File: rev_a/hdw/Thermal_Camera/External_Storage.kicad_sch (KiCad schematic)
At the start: 0 parts

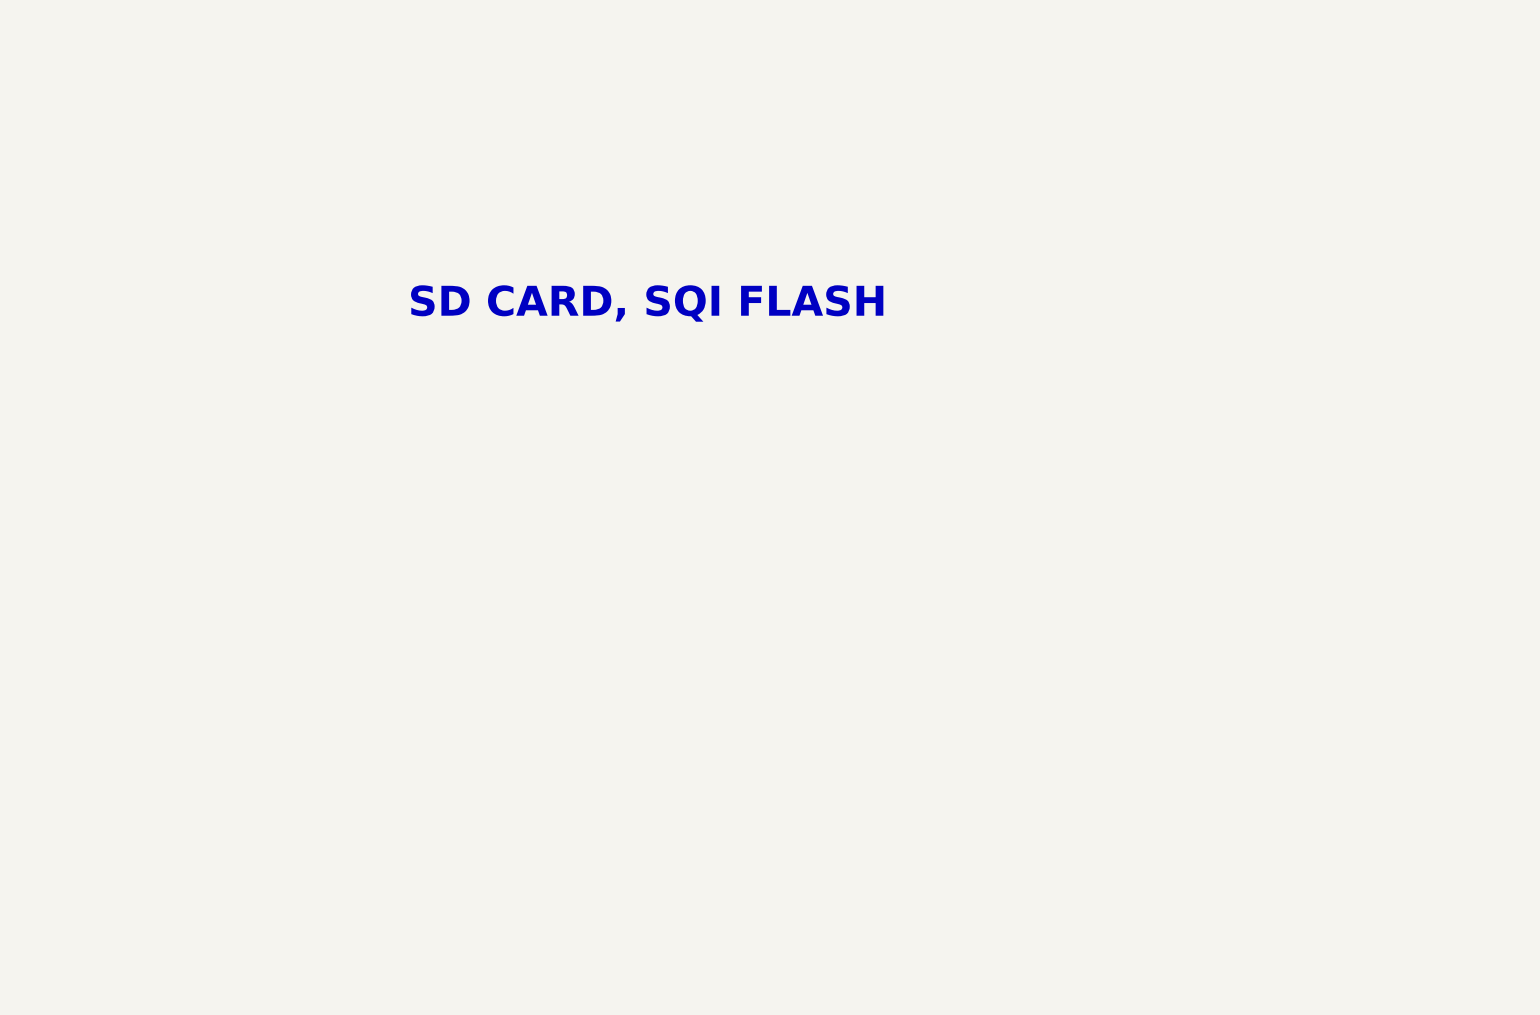
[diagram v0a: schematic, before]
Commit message: added lepton sensor, made some other schematic progress
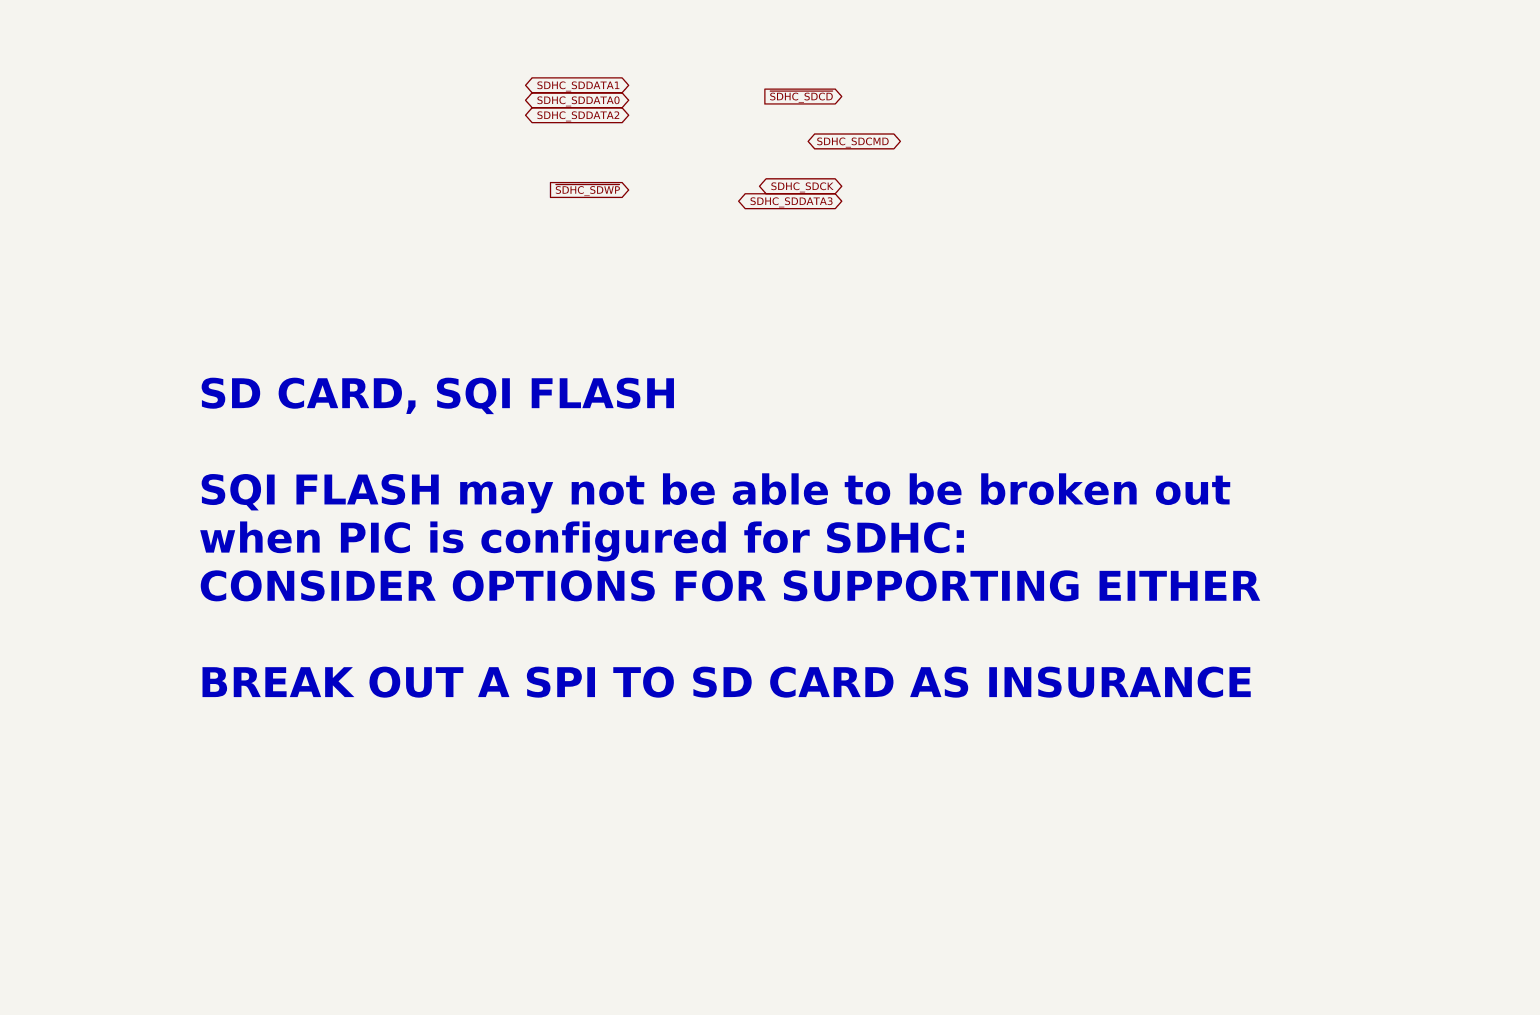
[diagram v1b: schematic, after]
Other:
- note added: "SD CARD, SQI FLASH SQI FLASH may not be able to be broken out when PIC is configured for SDHC: CONSIDER OPTIONS FOR SUPPORTING EITHER BREAK OUT A SPI TO SD CARD AS INSURANCE"
- note removed: "SD CARD, SQI FLASH"
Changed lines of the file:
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@@
   (title_block
     (title "Thermal Camera")
-    (date "2023-11-11")
+    (date "2023-11-12")
     (rev "PRELIM")
     (company "Drew Maatman and Michael Laffin")
   )
-  (text "SD CARD, SQI FLASH" (at 77.47 76.2 0)
+  (text "SD CARD, SQI FLASH\n\nSQI FLASH may not be able to be broken out\nwhen PIC is configured for SDHC:\nCONSIDER OPTIONS FOR SUPPORTING EITHER\n\nBREAK OUT A SPI TO SD CARD AS INSURANCE"
+    (at 41.91 140.97 0)
     (effects (font (face "Courier New") (size 5.08 5.08) (thickness 1.016) bold (color 194 0 0 1)) (justify left bottom))
   )
+  (global_label "~{SDHC_SDWP}" (shape input) (at 114.935 53.975 180) (fields_autoplaced)
+    (effects (font (size 1.27 1.27)) (justify right))
+    (property "Intersheetrefs" "${INTERSHEET_REFS}" (at 100.7013 53.975 0)
+      (effects (font (size 1.27 1.27)) (justify right) hide)
+    )
+  )
+  (global_label "SDHC_SDDATA1" (shape bidirectional) (at 114.935 36.195 180) (fields_autoplaced)
+    (effects (font (size 1.27 1.27)) (justify right))
+    (property "Intersheetrefs" "${INTERSHEET_REFS}" (at 96.6871 36.195 0)
+      (effects (font (size 1.27 1.27)) (justify right) hide)
+    )
+  )
+  (global_label "SDHC_SDCMD" (shape bidirectional) (at 145.415 45.72 0) (fields_autoplaced)
+    (effects (font (size 1.27 1.27)) (justify left))
+    (property "Intersheetrefs" "${INTERSHEET_REFS}" (at 162.03 45.72 0)
+      (effects (font (size 1.27 1.27)) (justify left) hide)
+    )
+  )
+  (global_label "SDHC_SDCK" (shape bidirectional) (at 151.13 53.34 180) (fields_autoplaced)
+    (effects (font (size 1.27 1.27)) (justify right))
+    (property "Intersheetrefs" "${INTERSHEET_REFS}" (at 135.9664 53.34 0)
+      (effects (font (size 1.27 1.27)) (justify right) hide)
+    )
+  )
+  (global_label "SDHC_SDDATA3" (shape bidirectional) (at 151.13 55.88 180) (fields_autoplaced)
+    (effects (font (size 1.27 1.27)) (justify right))
+    (property "Intersheetrefs" "${INTERSHEET_REFS}" (at 132.8821 55.88 0)
+      (effects (font (size 1.27 1.27)) (justify right) hide)
+    )
+  )
+  (global_label "SDHC_SDDATA0" (shape bidirectional) (at 114.935 38.735 180) (fields_autoplaced)
+    (effects (font (size 1.27 1.27)) (justify right))
+    (property "Intersheetrefs" "${INTERSHEET_REFS}" (at 96.6871 38.735 0)
+      (effects (font (size 1.27 1.27)) (justify right) hide)
+    )
+  )
+  (global_label "~{SDHC_SDCD}" (shape input) (at 151.13 38.1 180) (fields_autoplaced)
+    (effects (font (size 1.27 1.27)) (justify right))
+    (property "Intersheetrefs" "${INTERSHEET_REFS}" (at 137.0777 38.1 0)
+      (effects (font (size 1.27 1.27)) (justify right) hide)
+    )
+  )
+  (global_label "SDHC_SDDATA2" (shape bidirectional) (at 114.935 41.275 180) (fields_autoplaced)
+    (effects (font (size 1.27 1.27)) (justify right))
+    (property "Intersheetrefs" "${INTERSHEET_REFS}" (at 96.6871 41.275 0)
+      (effects (font (size 1.27 1.27)) (justify right) hide)
+    )
+  )
 )

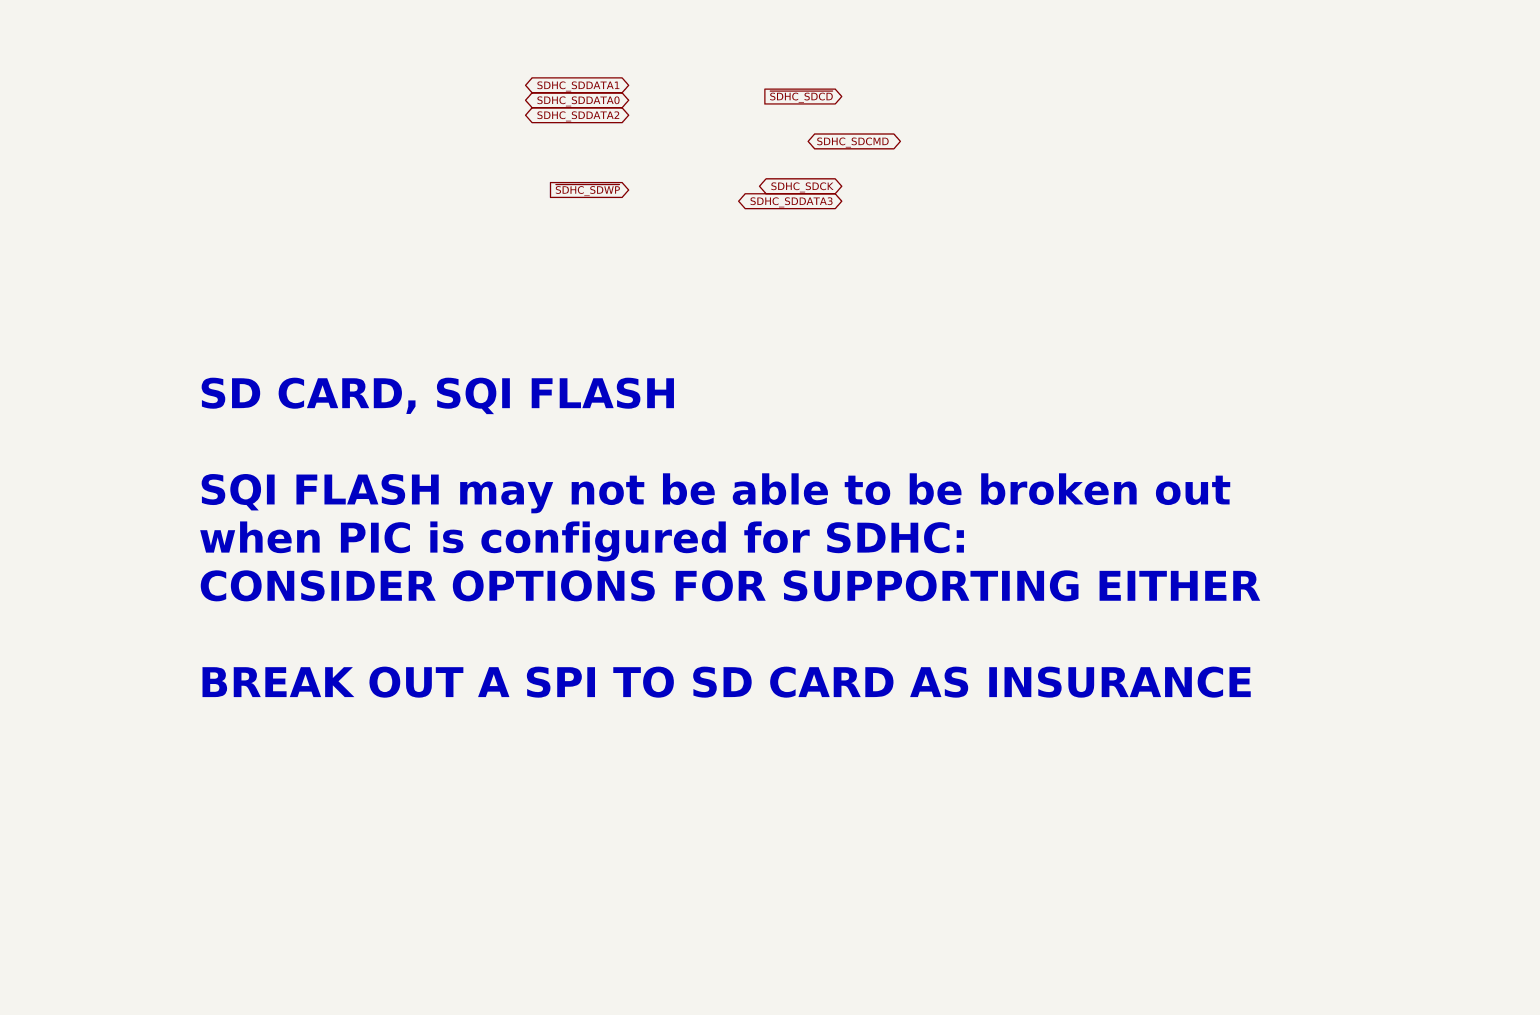
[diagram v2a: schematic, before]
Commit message: added SPI Flash and SD Card
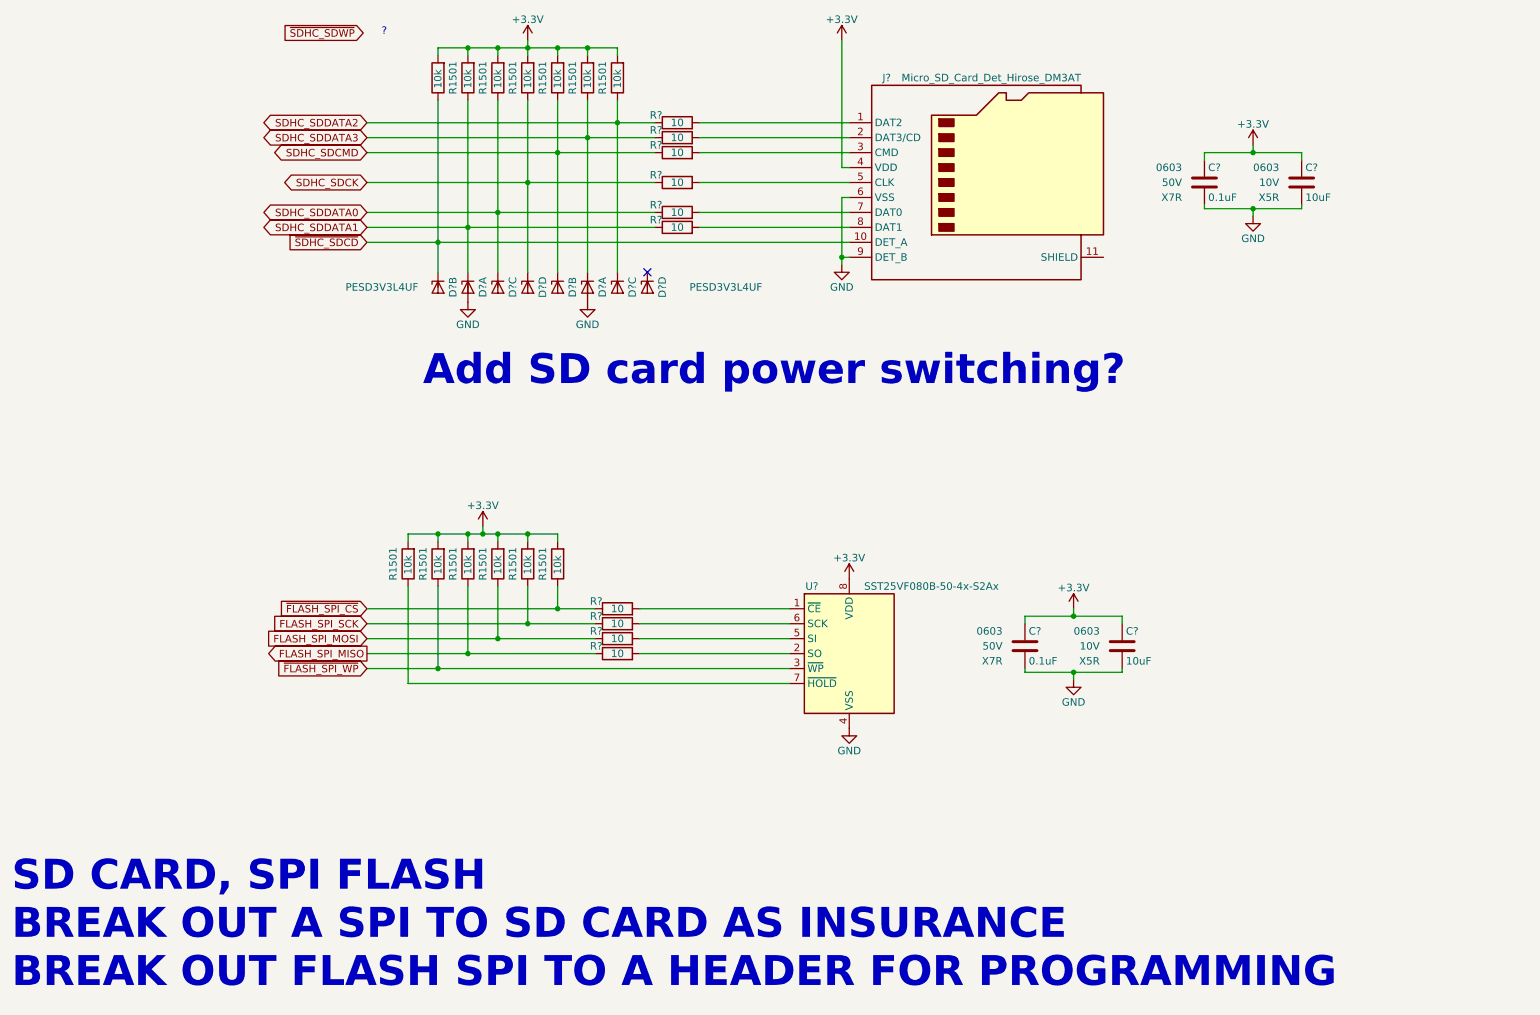
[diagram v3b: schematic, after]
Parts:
- added C? (x2): 10uF, Capacitors_SMD:C_0603, symbol Custom_Library:C_Custom
- added C? (x2): 0.1uF, Capacitors_SMD:C_0603, symbol Custom_Library:C_Custom
- added D? (x8): PESD3V3L4UF, Package_TO_SOT_SMD:SOT-886, symbol Power_Protection:PESD3V3L4UF
- added J?: Micro_SD_Card_Det_Hirose_DM3AT, Connectors_Card:Hirose_DM3AT-SF-PEJM5, symbol Connector:Micro_SD_Card_Det_Hirose_DM3AT
- added R1501 (x13): 10k, Resistors_SMD:R_0603, symbol Custom_Library:R_Custom
- added R? (x10): 10, Resistors_SMD:R_0603, symbol Custom_Library:R_Custom
- added U?: SST25VF080B-50-4x-S2Ax, Package_SO:SOIC-8_5.275x5.275mm_P1.27mm, symbol Memory_Flash:SST25VF080B-50-4x-S2Ax
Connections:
- net SDHC_SDCK: now also D?.6 (K4), R1501.2, R?.2
- net SDHC_SDCMD: now also D?.3 (K2), R1501.2, R?.2
- net SDHC_SDDATA0: now also D?.4 (K3), R1501.2, R?.2
- net SDHC_SDDATA1: now also D?.1 (K1), R1501.2, R?.2
- net SDHC_SDDATA2: now also D?.4 (K3), R1501.2, R?.2
- net SDHC_SDDATA3: now also D?.1 (K1), R1501.2, R?.2
- net ~{SDHC_SDCD}: now also D?.3 (K2), J?.10 (DET_A), R1501.2
- new net: R1501.2, U?.7 (~{HOLD})
- new net: J?.1 (DAT2), R?.1
- new net: R?.1, U?.6 (SCK)
- new net: R?.1, U?.5 (SI)
- new net: J?.2 (DAT3/CD), R?.1
- new net: J?.3 (CMD), R?.1
- new net: J?.5 (CLK), R?.1
- new net: J?.7 (DAT0), R?.1
- new net: J?.8 (DAT1), R?.1
- new net: R?.1, U?.1 (~{CE})
- new net: R?.1, U?.2 (SO)
- new net +3.3V: C?.1, C?.1, C?.1, C?.1, J?.4 (VDD), R1501.1, R1501.1, R1501.1, R1501.1, R1501.1, R1501.1, R1501.1, R1501.1, R1501.1, R1501.1, R1501.1, R1501.1, R1501.1, U?.8 (VDD)
- new net FLASH_SPI_MISO: R1501.2, R?.2
- new net FLASH_SPI_MOSI: R1501.2, R?.2
- new net FLASH_SPI_SCK: R1501.2, R?.2
- new net GND: C?.2, C?.2, C?.2, C?.2, D?.2 (A), D?.2 (A), D?.5 (A), D?.5 (A), J?.6 (VSS), J?.9 (DET_B), U?.4 (VSS)
- new net ~{FLASH_SPI_CS}: R1501.2, R?.2
- new net ~{FLASH_SPI_WP}: R1501.2, U?.3 (~{WP})
- no-connect marks 0 -> 1
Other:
- note added: "?"
- note added: "Add SD card power switching?"
- note added: "SD CARD, SPI FLASH BREAK OUT A SPI TO SD CARD AS INSURANCE BREAK OUT FLASH SPI TO A HEADER FOR PROGRAMMING"
- note removed: "SD CARD, SQI FLASH SQI FLASH may not be able to be broken out when PIC is configured for SDHC: CONSIDER OPTIONS FOR SUPPORTING EITHER BREAK OUT A SPI TO SD CARD AS INSURANCE"
